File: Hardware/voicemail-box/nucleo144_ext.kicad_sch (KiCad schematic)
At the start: 3 parts, among them J6 Micro_SD_Card_Det1

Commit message: ~ HW Configuration
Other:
- moved on the sheet: C3, J6, RN3

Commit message: ~working on first pcb-Draft
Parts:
- J6: footprint (none) -> Connector_Card:microSD_HC_Hirose_DM3AT-SF-PEJM5
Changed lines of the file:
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@@
 			)
 		)
-		(property "Footprint" ""
+		(property "Footprint" "Connector_Card:microSD_HC_Hirose_DM3AT-SF-PEJM5"
 			(at 166.37 34.29 0)
 			(effects

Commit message: schematic draft
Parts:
- renumbered C3 to C401, J6 to J401, RN3 to RN401
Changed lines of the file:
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@@
 		(on_board yes)
 		(dnp no)
-		(property "Reference" "C3"
+		(property "Reference" "C401"
 			(at 139.446 57.15 0)
 			(effects
@@
 			(project "voicemail-box"
 				(path "/e63e39d7-6ac0-4ffd-8aa3-1841a4541b55/7d1be1d6-550f-4338-bd10-7ce490ea6cc3"
-					(reference "C3")
+					(reference "C401")
 					(unit 1)
 				)
@@
 		(dnp no)
 		(fields_autoplaced yes)
-		(property "Reference" "RN3"
+		(property "Reference" "RN401"
 			(at 49.53 38.0999 0)
 			(effects
@@
 			(project "voicemail-box"
 				(path "/e63e39d7-6ac0-4ffd-8aa3-1841a4541b55/7d1be1d6-550f-4338-bd10-7ce490ea6cc3"
-					(reference "RN3")
+					(reference "RN401")
 					(unit 1)
 				)
@@
 		(dnp no)
 		(fields_autoplaced yes)
-		(property "Reference" "#PWR015"
+		(property "Reference" "#PWR0401"
 			(at 39.37 35.56 0)
 			(effects
@@
 			(project "voicemail-box"
 				(path "/e63e39d7-6ac0-4ffd-8aa3-1841a4541b55/7d1be1d6-550f-4338-bd10-7ce490ea6cc3"
-					(reference "#PWR015")
+					(reference "#PWR0401")
 					(unit 1)
 				)
@@
 		(dnp no)
 		(fields_autoplaced yes)
-		(property "Reference" "#PWR012"
+		(property "Reference" "#PWR0402"
 			(at 90.17 43.18 0)
 			(effects
@@
 			(project "voicemail-box"
 				(path "/e63e39d7-6ac0-4ffd-8aa3-1841a4541b55/7d1be1d6-550f-4338-bd10-7ce490ea6cc3"
-					(reference "#PWR012")
+					(reference "#PWR0402")
 					(unit 1)
 				)
@@
 		(dnp no)
 		(fields_autoplaced yes)
-		(property "Reference" "#PWR016"
+		(property "Reference" "#PWR0404"
 			(at 138.43 57.15 0)
 			(effects
@@
 			(project "voicemail-box"
 				(path "/e63e39d7-6ac0-4ffd-8aa3-1841a4541b55/7d1be1d6-550f-4338-bd10-7ce490ea6cc3"
-					(reference "#PWR016")
+					(reference "#PWR0404")
 					(unit 1)
 				)
@@
 		(dnp no)
 		(fields_autoplaced yes)
-		(property "Reference" "#PWR019"
+		(property "Reference" "#PWR0403"
 			(at 90.17 73.66 0)
 			(effects
@@
 			(project "voicemail-box"
 				(path "/e63e39d7-6ac0-4ffd-8aa3-1841a4541b55/7d1be1d6-550f-4338-bd10-7ce490ea6cc3"
-					(reference "#PWR019")
+					(reference "#PWR0403")
 					(unit 1)
 				)
@@
 		(dnp no)
 		(fields_autoplaced yes)
-		(property "Reference" "#PWR014"
+		(property "Reference" "#PWR0405"
 			(at 138.43 73.66 0)
 			(effects
@@
 			(project "voicemail-box"
 				(path "/e63e39d7-6ac0-4ffd-8aa3-1841a4541b55/7d1be1d6-550f-4338-bd10-7ce490ea6cc3"
-					(reference "#PWR014")
+					(reference "#PWR0405")
 					(unit 1)
 				)
@@
 		(dnp no)
 		(fields_autoplaced yes)
-		(property "Reference" "J6"
+		(property "Reference" "J401"
 			(at 114.935 30.48 0)
 			(effects
@@
 			(project "voicemail-box"
 				(path "/e63e39d7-6ac0-4ffd-8aa3-1841a4541b55/7d1be1d6-550f-4338-bd10-7ce490ea6cc3"
-					(reference "J6")
-					(unit 1)
-				)
+					(reference "J401")
+					(unit 1)
+				)

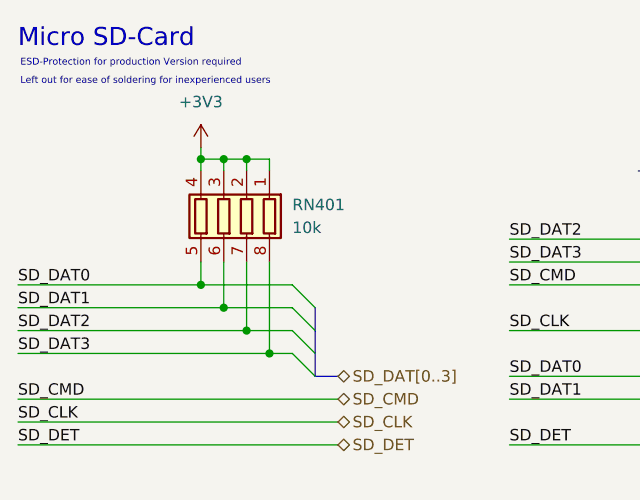
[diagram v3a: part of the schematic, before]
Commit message: HW Layout progress todo: + Antenna + Audio Jacks + Planes (Supply only)
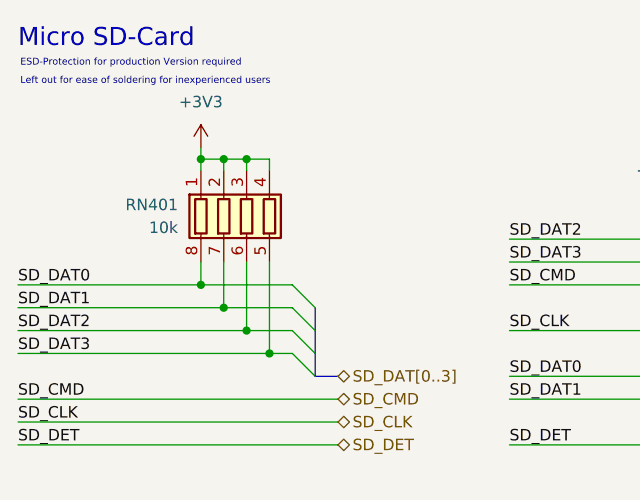
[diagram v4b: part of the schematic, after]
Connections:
- net SD_DAT0: now also RN401.8 (R1.2); no longer RN401.5 (R4.2)
- net SD_DAT1: now also RN401.7 (R2.2); no longer RN401.6 (R3.2)
- net SD_DAT2: now also RN401.6 (R3.2); no longer RN401.7 (R2.2)
- net SD_DAT3: now also RN401.5 (R4.2); no longer RN401.8 (R1.2)
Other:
- moved on the sheet: RN401
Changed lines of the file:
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@@
 	(symbol
 		(lib_id "Device:R_Pack04")
-		(at 41.91 39.37 180)
+		(at 44.45 39.37 0)
+		(mirror x)
 		(unit 1)
 		(exclude_from_sim no)
@@
 		(on_board yes)
 		(dnp no)
-		(fields_autoplaced yes)
 		(property "Reference" "RN401"
-			(at 49.53 38.0999 0)
+			(at 36.83 38.0999 0)
 			(effects
 				(font
@@
 		)
 		(property "Value" "10k"
-			(at 49.53 40.6399 0)
+			(at 36.83 40.6399 0)
 			(effects
 				(font
@@
 		)
 		(property "Footprint" "Resistor_SMD:R_Array_Convex_4x0603"
-			(at 34.925 39.37 90)
+			(at 51.435 39.37 90)
 			(effects
 				(font
@@
 		)
 		(property "Datasheet" "~"
-			(at 41.91 39.37 0)
+			(at 44.45 39.37 0)
 			(effects
 				(font
@@
 		)
 		(property "Description" "4 resistor network, parallel topology"
-			(at 41.91 39.37 0)
+			(at 44.45 39.37 0)
 			(effects
 				(font

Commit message: ~layout
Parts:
- added R506, R507: 10k, Resistor_SMD:R_0805_2012Metric_Pad1.20x1.40mm_HandSolder, symbol Device:R
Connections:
- net +3V3: now also R506.1, R507.1
- net SD_CMD: now also R506.2
- net SD_DET: now also R507.2
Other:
- note added: "Dected = low active"
- moved on the sheet: C401, J401, RN401
